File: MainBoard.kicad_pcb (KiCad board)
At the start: 2 copper layers, 100 parts, among them J1 USB B Mini, J5 Audio Out Port, P1 CARTRIDGE_SLOT, P2 FRONT_PANEL_CONNECTOR, P4 Multi AV Out, Q1 2SC4699, SW1 RESET, U1 S-CPU, U11 PST529D, U13 S-SMP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

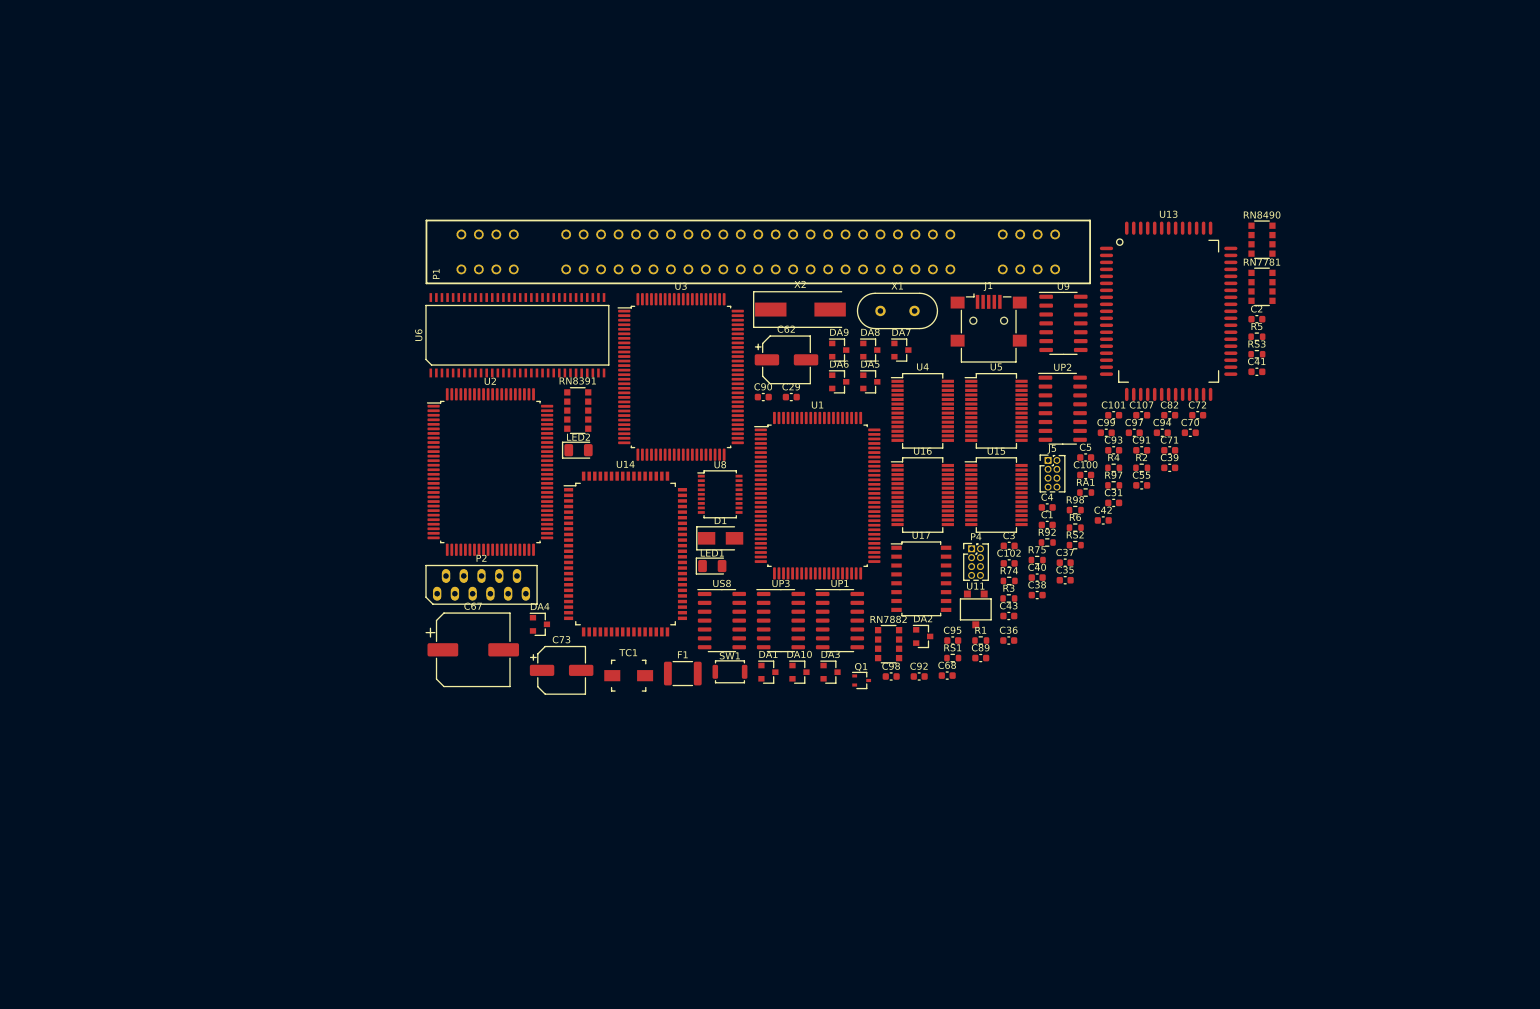
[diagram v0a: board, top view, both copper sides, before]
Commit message: Reassigned footprints and 3D models
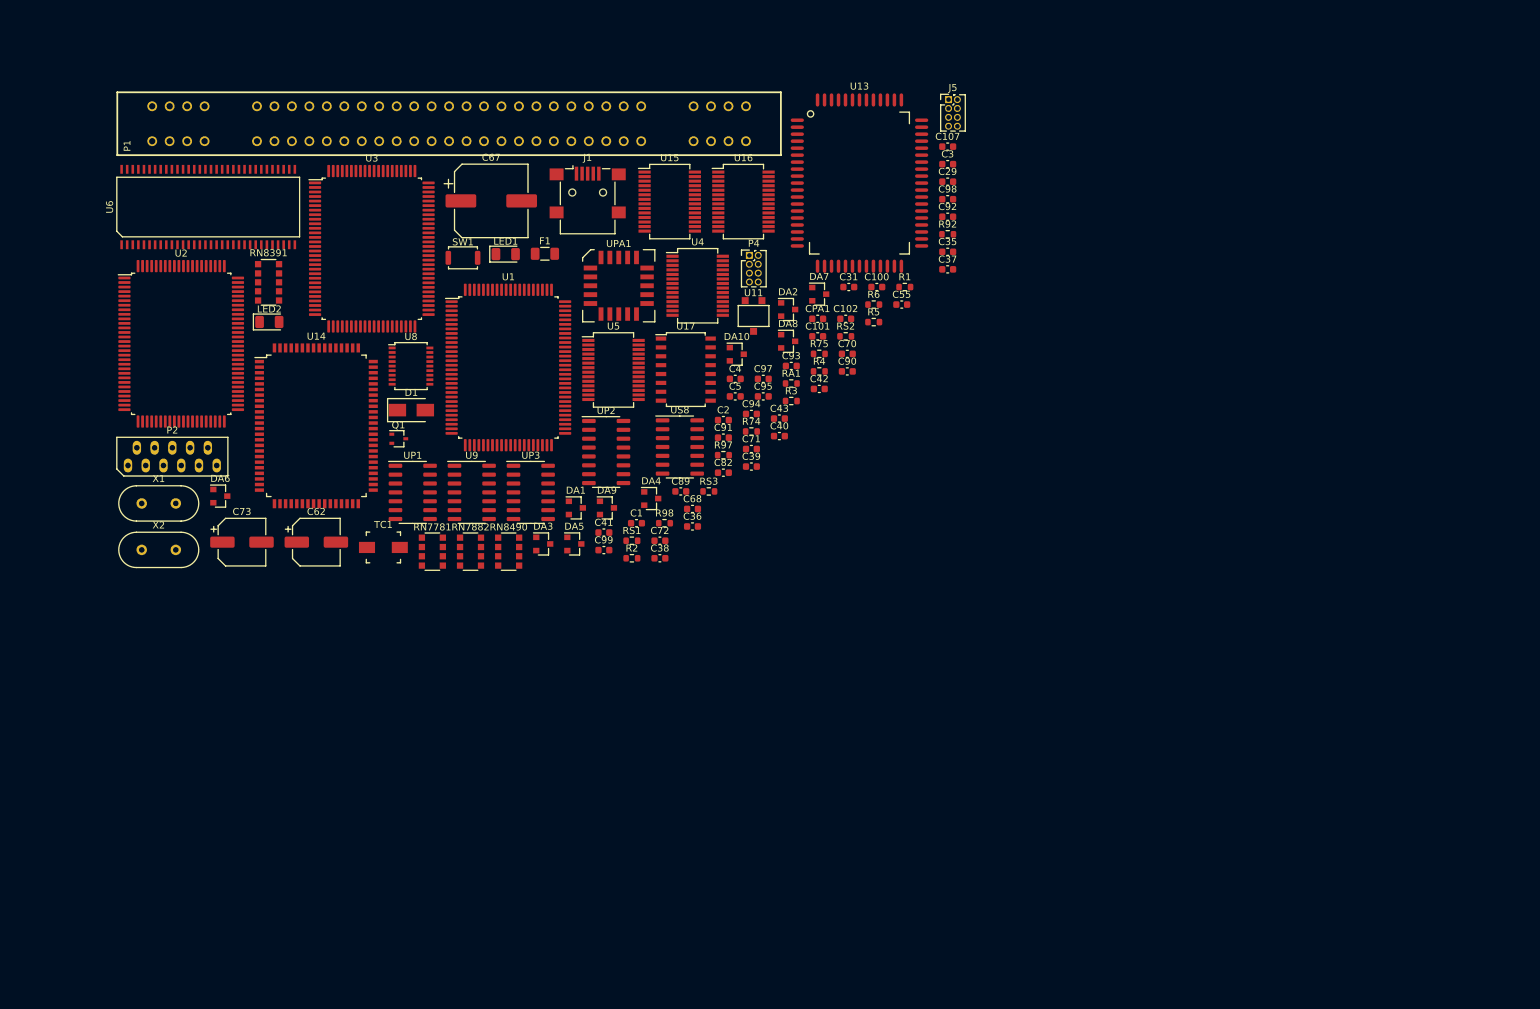
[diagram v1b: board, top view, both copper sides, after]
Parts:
- added CPA1: 100nF, Capacitor_SMD:C_0603_1608Metric, F.Cu at (135.0, 63.2)
- added UPA1: 16V8, SNES:PLCC-20, F.Cu at (106.6, 58.5)
- F1: footprint Fuse:Fuse_1812_4532Metric -> Fuse:Fuse_1206_3216Metric
- SW1: footprint Button_Switch_SMD:SW_Push_SPST_NO_Alps_SKRK -> SNES:SW_Push_SPST_NO_Alps_SKRK
- X2: footprint Crystal:Crystal_SMD_HC49-SD -> Crystal:Crystal_HC49-4H_Vertical
- moved RN7781 124.7 mm to (79.9, 96.5)
- moved RN8490 116.7 mm to (90.8, 96.5)
- moved X1 109.3 mm to (38.3, 89.6)
- moved X2 100.4 mm to (38.3, 96.3)
- moved C41 96.3 mm to (104.4, 93.8)
- moved DA6 90.1 mm to (49.5, 88.6)
- moved U9 88.1 mm to (85.5, 88.0)
- moved RS3 80.9 mm to (119.4, 87.9)
- moved C72 79.1 mm to (112.4, 95.0)
- moved C2 77.7 mm to (121.5, 77.7)
- moved Q1 74.8 mm to (75.1, 80.4)
- moved R2 74.1 mm to (108.4, 97.5)
- moved C99 73.9 mm to (104.4, 96.3)
- moved C62 72.2 mm to (63.3, 95.2)
- moved SW1 70.5 mm to (84.3, 54.5)
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
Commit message: S-CPU and S-WRAM mostly wired
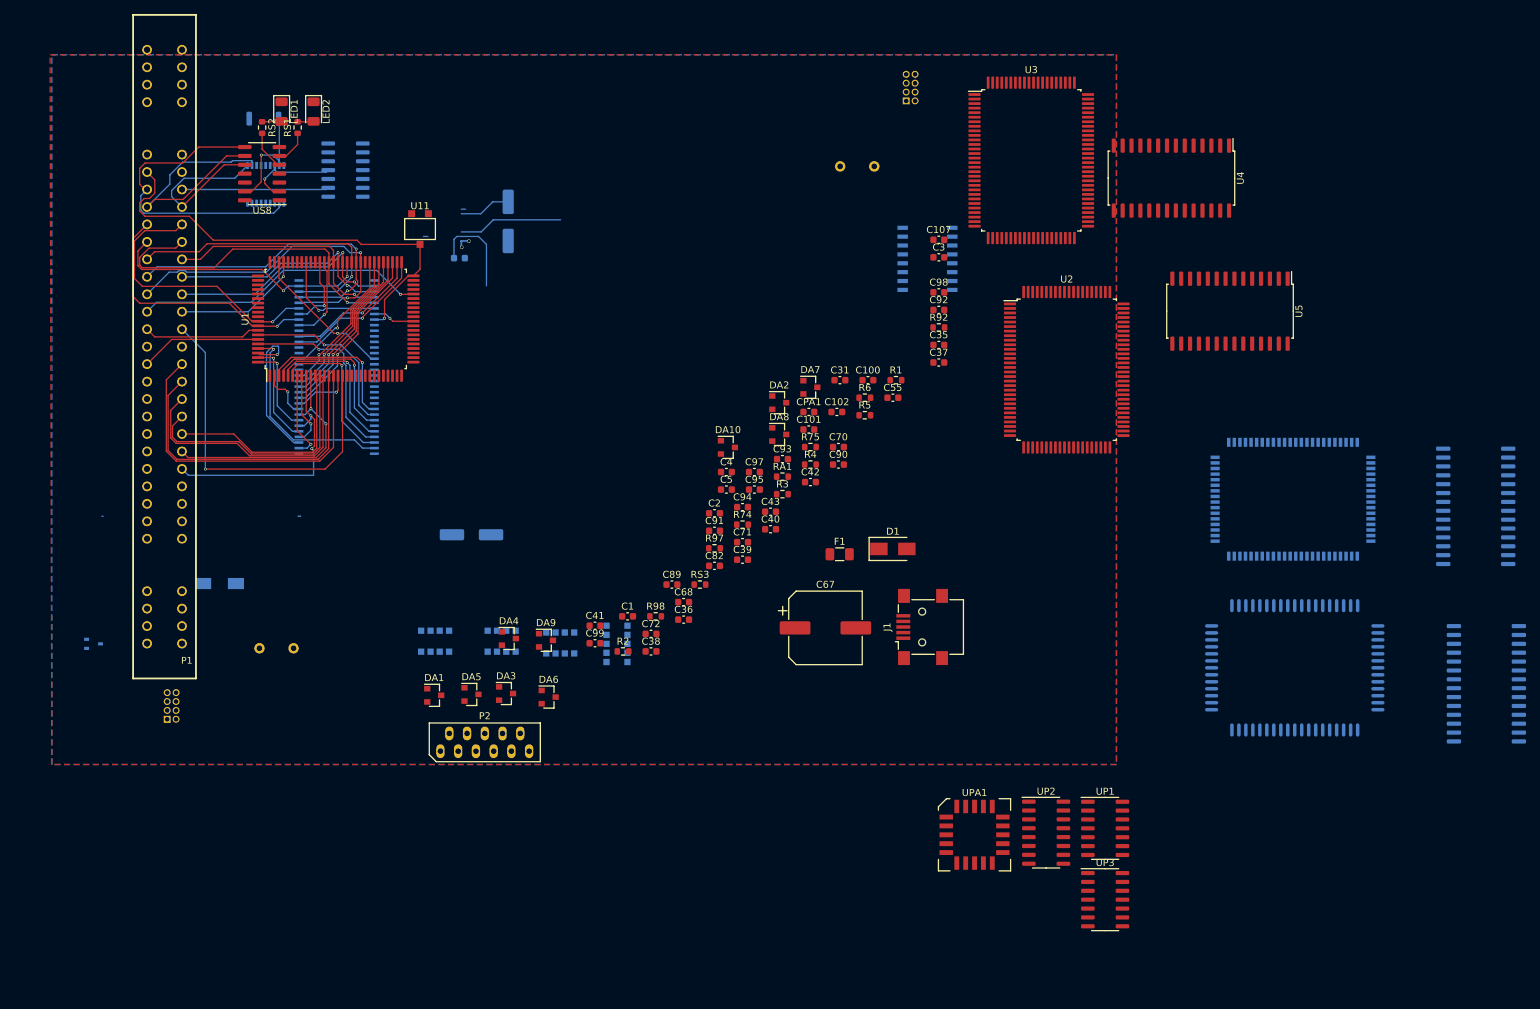
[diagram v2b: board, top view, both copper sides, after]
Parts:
- C29, C62, C73, J5, P4, Q1, RN7781, RN7882, RN8391, RN8490, SW1, TC1, U13, U14, U17, U6, U8, U9, X1, X2: moved to B.Cu
- U15: footprint Package_SO:SSOP-28_5.3x10.2mm_P0.65mm -> SNES:SOIC-28W_7.5x17.9mm_P1.27mm; moved to B.Cu
- U16: footprint SNES:SSOP-28_5.3x10.2mm_P0.65mm -> SNES:SOIC-28W_7.5x17.9mm_P1.27mm; moved to B.Cu
- U4, U5: footprint SNES:SSOP-28_5.3x10.2mm_P0.65mm -> SNES:SOIC-28W_7.5x17.9mm_P1.27mm
- moved J5 142.8 mm to (41.9, 120.5)
- moved U14 140.2 mm to (203.1, 89.0), turned to 270 degrees
- moved U15 135.8 mm to (230.8, 115.4), turned to 180 degrees
- moved U2 126.8 mm to (170.7, 70.5)
- moved X2 114.1 mm to (138.3, 41.4)
- moved U16 113.5 mm to (229.2, 90.0)
- moved UP1 110.2 mm to (176.2, 136.1)
- moved UP3 100.8 mm to (176.2, 146.3)
- moved U3 95.2 mm to (165.6, 40.5)
- moved UPA1 93.7 mm to (157.5, 137.1)
- moved U13 93.3 mm to (203.3, 113.2), turned to 270 degrees
- moved RS2 88.7 mm to (55.5, 35.8), turned to 270 degrees
- moved U5 88.7 mm to (194.1, 62.1), turned to 270 degrees
- moved UP2 83.3 mm to (167.7, 136.8)
- moved J1 78.5 mm to (150.0, 107.3), turned to 90 degrees
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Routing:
- net /~RESOUT1: track 0.00 -> 64.1 mm, vias 0 -> 1
- net /CA23: track 0.00 -> 53.0 mm, vias 0 -> 1
- net /D0: track 0.00 -> 49.1 mm, vias 0 -> 2
- net /CA21: track 0.00 -> 49.0 mm
- net /D7: track 0.00 -> 48.7 mm, vias 0 -> 1
- net /D1: track 0.00 -> 46.3 mm, vias 0 -> 2
- net /CA20: track 0.00 -> 45.3 mm
- net /CIC2: track 0.00 -> 44.9 mm
- net /D2: track 0.00 -> 43.1 mm, vias 0 -> 1
- net /~IRQ: track 0.00 -> 42.0 mm, vias 0 -> 1
- net /~CPUWR: track 0.00 -> 40.1 mm, vias 0 -> 1
- net /CA19: track 0.00 -> 39.9 mm
- net /D3: track 0.00 -> 38.3 mm, vias 0 -> 2
- net /~CPURD: track 0.00 -> 37.1 mm, vias 0 -> 1
- net /CIC0: track 0.00 -> 36.9 mm
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- added copper zone on F.Cu, net GND
- added copper zone on B.Cu, net VCC
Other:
- copper layers 2 -> 4
- net class Default: clearance 0.2 -> 0.127; trace_width 0.25 -> 0.127; via_dia 0.8 -> 0.4; via_drill 0.4 -> 0.25
- net class Power added: clearance 0.127, trace_width 0.508, via_dia 0.508, via_drill 0.25
- rule trace_clearance: 0.2 -> 0.127
- rule trace_min: 0.2 -> 0.08
- rule via_min_drill: 0.3 -> 0.25

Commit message: Properly laid out XIN and Gamepad portions, the rest is WIP
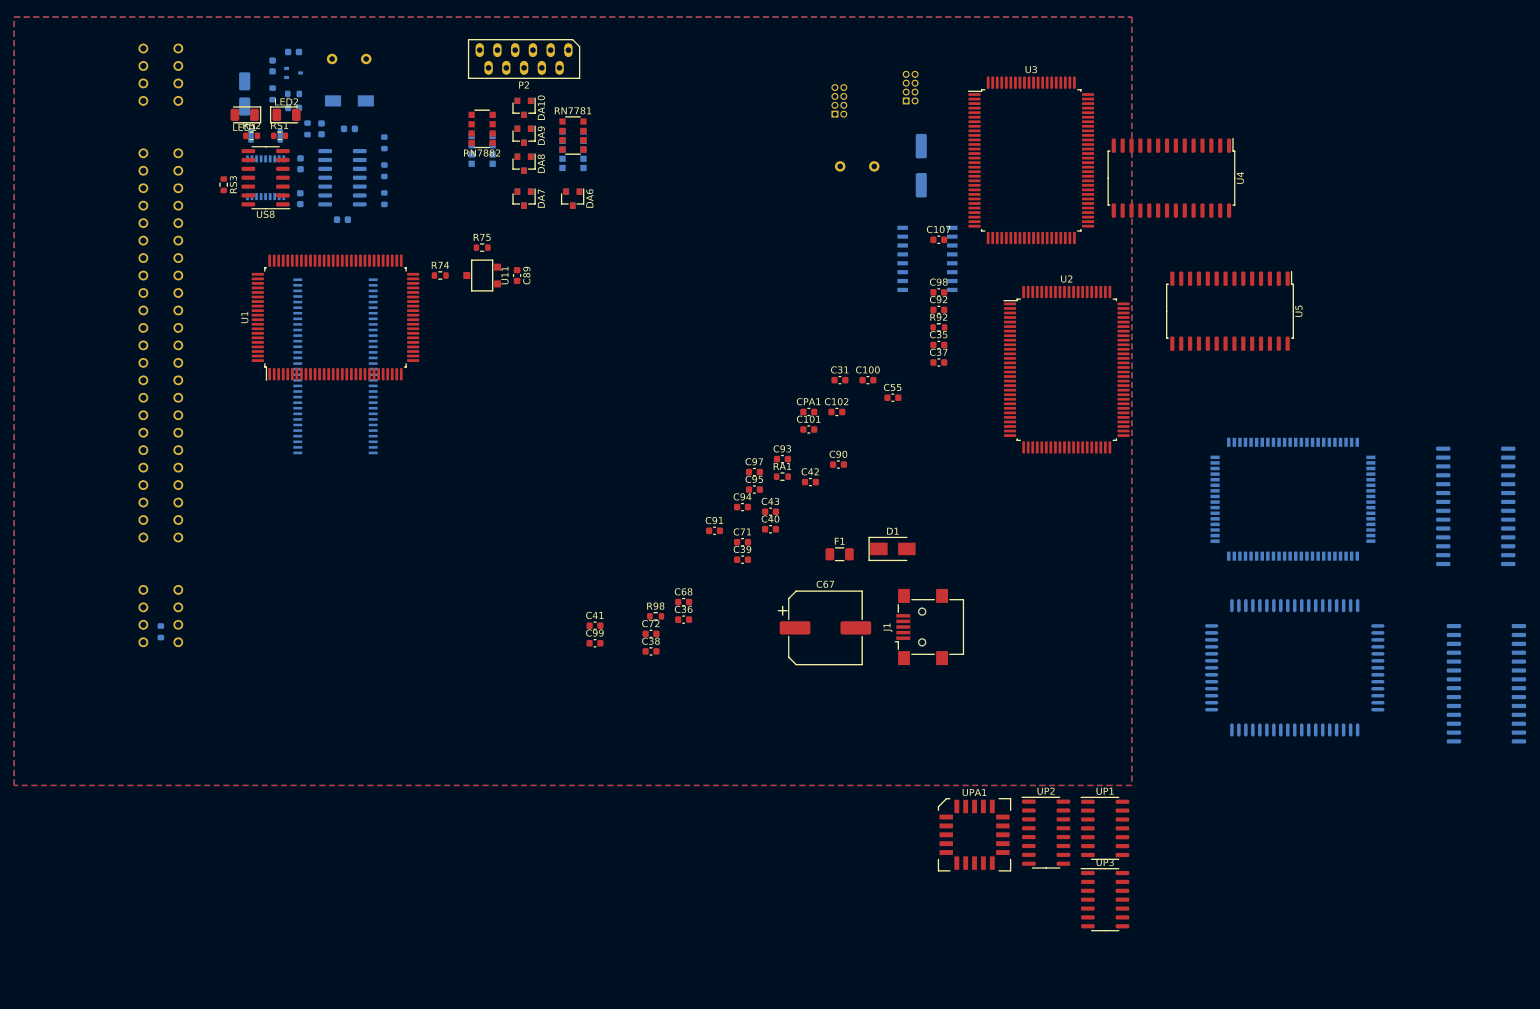
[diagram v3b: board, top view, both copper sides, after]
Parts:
- C1, C2, C3, C4, C5, C70, C82, DA1, DA2, DA3, DA4, DA5, P1, R1, R2, R3, R4, R5, R6, R97: moved to B.Cu
- C62: footprint Capacitor_SMD:CP_Elec_6.3x5.4 -> Capacitor_SMD:CP_Elec_4x5.4
- RN7781, RN7882: moved to F.Cu
- moved J5 129.0 mm to (137.5, 33.9)
- moved P2 98.0 mm to (93.0, 26.0), turned to 180 degrees
- moved R1 95.5 mm to (60.0, 31.0)
- moved C3 94.8 mm to (60.0, 33.0), turned to 180 degrees
- moved R2 94.3 mm to (57.0, 31.0), turned to 90 degrees
- moved C1 93.9 mm to (60.0, 25.0), turned to 180 degrees
- moved RS3 89.0 mm to (50.0, 44.0), turned to 270 degrees
- moved C5 88.9 mm to (57.0, 27.0), turned to 90 degrees
- moved Q1 86.6 mm to (60.0, 28.0)
- moved R3 85.8 mm to (62.0, 36.0), turned to 270 degrees
- moved X1 85.7 mm to (70.4, 26.0), turned to 180 degrees
- moved C70 84.8 mm to (61.0, 46.0), turned to 270 degrees
- moved DA5 84.3 mm to (93.0, 33.0), turned to 270 degrees
- moved C73 83.3 mm to (149.9, 41.3), turned to 90 degrees
- moved R97 80.2 mm to (41.0, 108.0), turned to 90 degrees
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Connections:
- RN7882 pad 1: /JPIO7 -> /4016.D1
- RN7882 pad 3: /4016.D1 -> /JPIO7
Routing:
- net /~RESOUT1: track 64.1 -> 0.00 mm, vias 1 -> 0
- net /CA23: track 53.0 -> 0.00 mm, vias 1 -> 0
- net /D0: track 49.1 -> 0.00 mm, vias 2 -> 0
- net /CA21: track 49.0 -> 0.00 mm
- net /D7: track 48.7 -> 0.00 mm, vias 1 -> 0
- net /D1: track 46.3 -> 0.00 mm, vias 2 -> 0
- net /CA20: track 45.3 -> 0.00 mm
- net /CIC2: track 44.9 -> 0.00 mm
- net /D2: track 43.1 -> 0.00 mm, vias 1 -> 0
- net /~IRQ: track 42.0 -> 0.00 mm, vias 1 -> 0
- net /~CPUWR: track 40.1 -> 0.00 mm, vias 1 -> 0
- net /CA19: track 39.9 -> 0.00 mm
- net /D3: track 38.3 -> 0.00 mm, vias 2 -> 0
- net /~CPURD: track 37.1 -> 0.00 mm, vias 1 -> 0
- net /CIC0: track 36.9 -> 0.00 mm
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- added copper zone on B.Cu, net GND
- added copper zone on F.Cu, net VCC
- removed copper zone on F.Cu, net GND
- removed copper zone on B.Cu, net VCC
